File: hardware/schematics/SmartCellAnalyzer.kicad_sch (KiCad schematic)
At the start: 20 parts, among them Q1 2N7000, Q2 PMOS, Q3 IRF4905, Q4 PMOS, U1 RP2040, U2 PCA9685PW, U3 INA3221, U4 XL4015

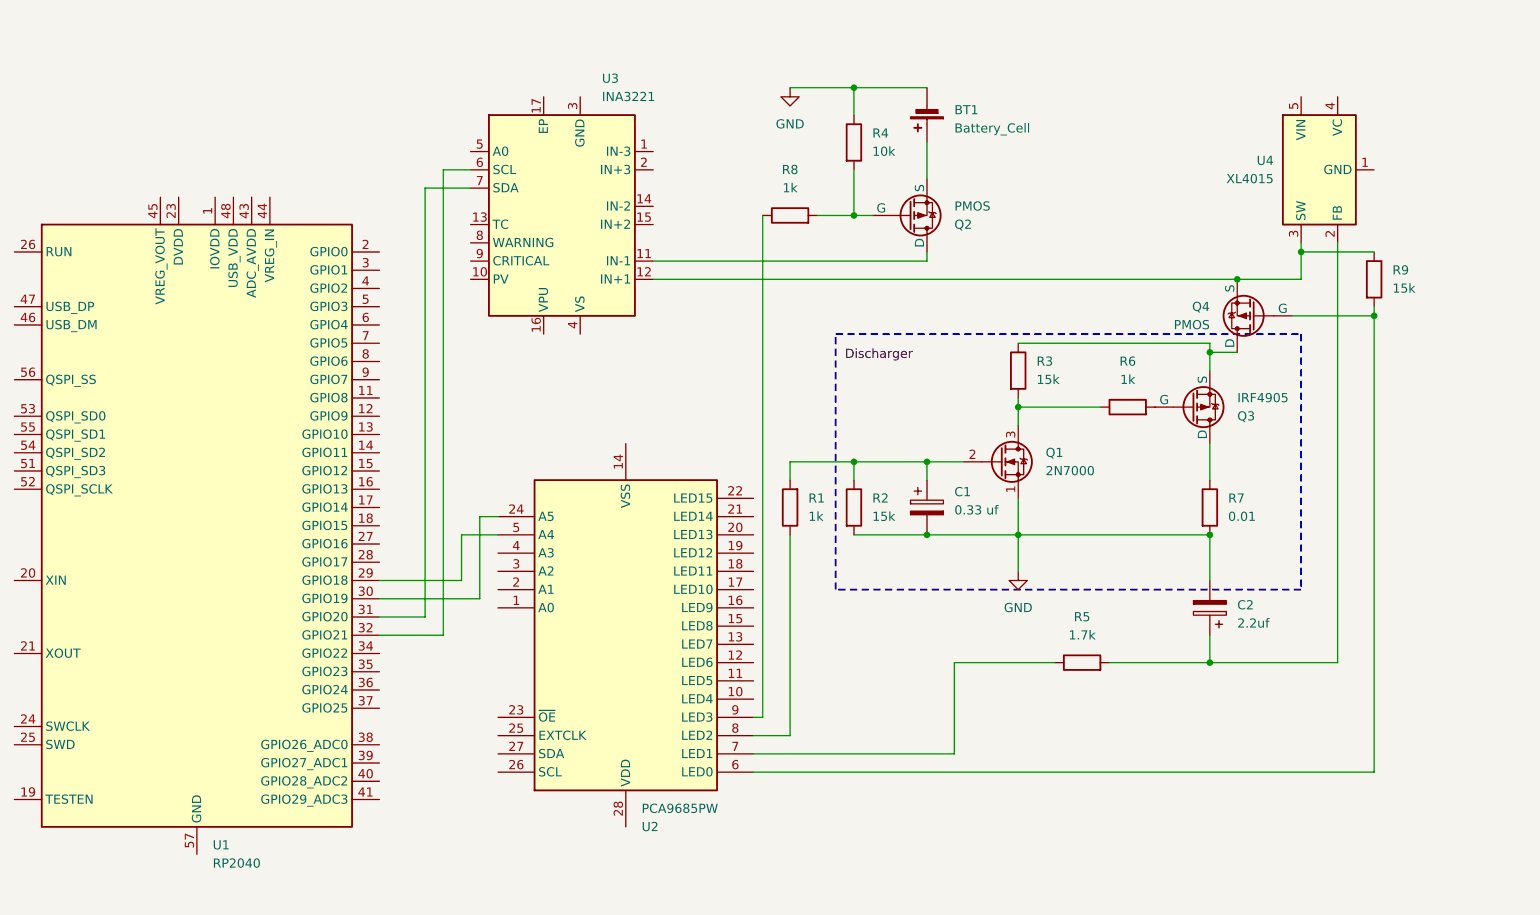
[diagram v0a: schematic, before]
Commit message: docs: refresh schematic documentation and assets
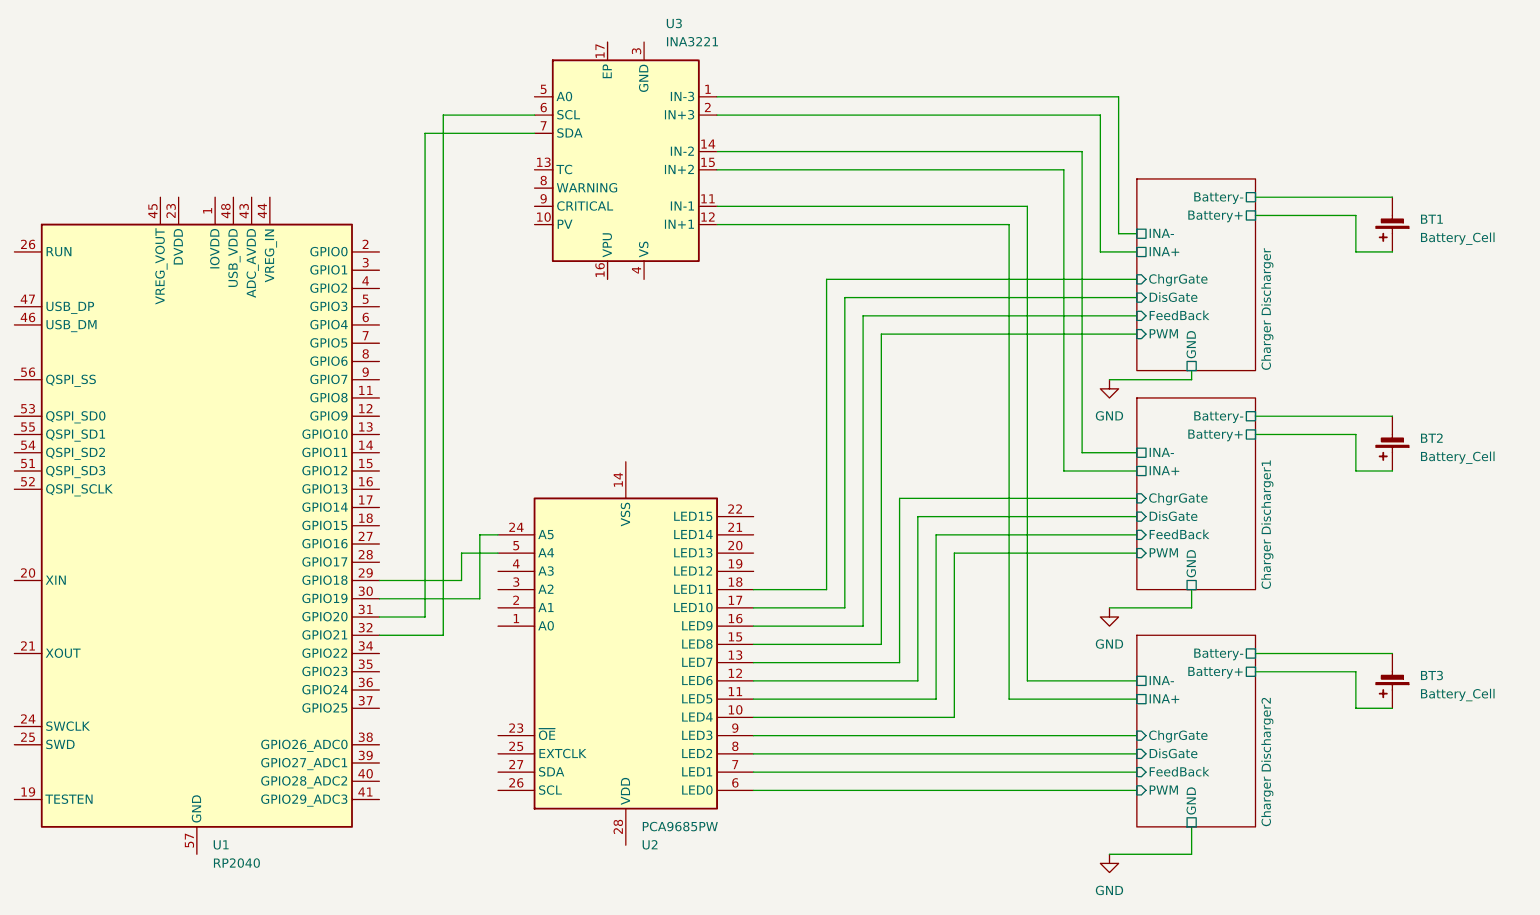
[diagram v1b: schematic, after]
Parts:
- removed C1: 0.33 uf, symbol Device:C_Polarized
- removed C2: 2.2uf, symbol Device:C_Polarized
- removed Q1: 2N7000, Package_TO_SOT_THT:TO-92_Inline, symbol Transistor_FET:2N7000
- removed Q2, Q4: PMOS, symbol Simulation_SPICE:PMOS
- removed Q3: IRF4905, symbol Simulation_SPICE:PMOS
- removed R1, R6, R8: 1k, symbol Device:R
- removed R2, R3, R9: 15k, symbol Device:R
- removed R4: 10k, symbol Device:R
- removed R5: 1.7k, symbol Device:R
- removed R7: 0.01, symbol Device:R
- removed U4: XL4015, Package_TO_SOT_SMD:TO-263-5_TabPin3, symbol Regulator_Switching:XL4015
- added BT2, BT3: Battery_Cell, symbol Device:Battery_Cell
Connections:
- net GND: no longer BT1.2 (-)
- net Charger Discharger2/INA+: now reaches U3.12 (IN+1)
- net Charger Discharger2/PWM: now reaches U2.6 (LED0)
- net Charger Discharger2/DisGate: now reaches U2.8 (LED2)
- net Charger Discharger1/PWM: now reaches U2.10 (LED4)
- net Charger Discharger1/FeedBack: now reaches U2.11 (LED5)
- net Charger Discharger1/DisGate: now reaches U2.12 (LED6)
- net Charger Discharger1/ChgrGate: now reaches U2.13 (LED7)
- net Charger Discharger/PWM: now reaches U2.15 (LED8)
- net Charger Discharger/FeedBack: now reaches U2.16 (LED9)
- net Charger Discharger/DisGate: now reaches U2.17 (LED10)
- net Charger Discharger/ChgrGate: now reaches U2.18 (LED11)
- net Charger Discharger2/FeedBack: now reaches U2.7 (LED1)
- net Charger Discharger2/ChgrGate: now reaches U2.9 (LED3)
- net Charger Discharger/INA-: now reaches U3.1 (IN-3)
- net Charger Discharger2/INA-: now reaches U3.11 (IN-1)
- net Charger Discharger1/INA-: now reaches U3.14 (IN-2)
- net Charger Discharger1/INA+: now reaches U3.15 (IN+2)
- net Charger Discharger/INA+: now reaches U3.2 (IN+3)
- net Charger Discharger/Battery+: now reaches BT1.1 (+)
- new net Charger Discharger/Battery-: BT1.2 (-)
- new net Charger Discharger1/Battery+: BT2.1 (+)
- new net Charger Discharger1/Battery-: BT2.2 (-)
- new net Charger Discharger2/Battery+: BT3.1 (+)
- new net Charger Discharger2/Battery-: BT3.2 (-)
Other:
- added sheet Charger Discharger (ChrgerDischarger.kicad_sch)
- added sheet Charger Discharger1 (ChrgerDischarger.kicad_sch)
- added sheet Charger Discharger2 (ChrgerDischarger.kicad_sch)
- title: (none) -> Smart Cell Analizer
- moved on the sheet: BT1, U2, U3
